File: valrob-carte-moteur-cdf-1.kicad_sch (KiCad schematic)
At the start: 0 parts

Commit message: schem: add ESP32-S3-WROOM-1 symbol
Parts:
- added U1: ESP32-S3-WROOM-1, PCM_Espressif:ESP32-S3-WROOM-1, symbol PCM_Espressif:ESP32-S3-WROOM-1
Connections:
- new net GND: U1.1 (GND), U1.40 (GND), U1.41 (GND)
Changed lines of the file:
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@@
 	(generator_version "9.0")
 	(paper "A4")
+	(wire
+		(pts
+			(xy 134.62 133.35) (xy 134.62 135.89)
+		)
+		(stroke
+			(width 0)
+			(type default)
+		)
+	)
+	(symbol
+		(lib_id "PCM_Espressif:ESP32-S3-WROOM-1")
+		(at 134.62 92.71 0)
+		(unit 1)
+		(exclude_from_sim no)
+		(in_bom yes)
+		(on_board yes)
+		(dnp no)
+		(fields_autoplaced yes)
+		(property "Reference" "U1"
+			(at 136.7633 49.53 0)
+			(effects
+				(font
+					(size 1.27 1.27)
+				)
+				(justify left)
+			)
+		)
+		(property "Value" "ESP32-S3-WROOM-1"
+			(at 136.7633 52.07 0)
+			(effects
+				(font
+					(size 1.27 1.27)
+				)
+				(justify left)
+			)
+		)
+		(property "Footprint" "PCM_Espressif:ESP32-S3-WROOM-1"
+			(at 137.16 140.97 0)
+			(effects
+				(font
+					(size 1.27 1.27)
+				)
+				(hide yes)
+			)
+		)
+		(property "Datasheet" "https://www.espressif.com/sites/default/files/documentation/esp32-s3-wroom-1_wroom-1u_datasheet_en.pdf"
+			(at 137.16 143.51 0)
+			(effects
+				(font
+					(size 1.27 1.27)
+				)
+				(hide yes)
+			)
+		)
+		(property "Description" "2.4 GHz WiFi (802.11 b/g/n) and Bluetooth ® 5 (LE) module Built around ESP32S3 series of SoCs, Xtensa ® dualcore 32bit LX7 microprocessor Flash up to 16 MB, PSRAM up to 8 MB 36 GPIOs, rich set of peripherals Onboard PCB antenna"
+			(at 134.62 92.71 0)
+			(effects
+				(font
+					(size 1.27 1.27)
+				)
+				(hide yes)
+			)
+		)
+		(pin "32"
+		)
+		(pin "2"
+		)
+		(pin "5"
+		)
+		(pin "1"
+		)
+		(pin "17"
+		)
+		(pin "31"
+		)
+		(pin "15"
+		)
+		(pin "19"
+		)
+		(pin "14"
+		)
+		(pin "20"
+		)
+		(pin "23"
+		)
+		(pin "30"
+		)
+		(pin "13"
+		)
+		(pin "3"
+		)
+		(pin "16"
+		)
+		(pin "25"
+		)
+		(pin "18"
+		)
+		(pin "4"
+		)
+		(pin "34"
+		)
+		(pin "33"
+		)
+		(pin "40"
+		)
+		(pin "6"
+		)
+		(pin "29"
+		)
+		(pin "8"
+		)
+		(pin "38"
+		)
+		(pin "36"
+		)
+		(pin "9"
+		)
+		(pin "22"
+		)
+		(pin "21"
+		)
+		(pin "12"
+		)
+		(pin "7"
+		)
+		(pin "11"
+		)
+		(pin "10"
+		)
+		(pin "24"
+		)
+		(pin "26"
+		)
+		(pin "28"
+		)
+		(pin "39"
+		)
+		(pin "41"
+		)
+		(pin "27"
+		)
+		(pin "35"
+		)
+		(pin "37"
+		)
+		(instances
+			(project ""
+				(path "/b89f538c-def5-4450-bb35-40e96c574400"
+					(reference "U1")
+					(unit 1)
+				)
+			)
+		)
+	)
+	(symbol
+		(lib_id "power:GND")
+		(at 134.62 135.89 0)
+		(unit 1)
+		(exclude_from_sim no)
+		(in_bom yes)
+		(on_board yes)
+		(dnp no)
+		(fields_autoplaced yes)
+		(property "Reference" "#PWR01"
+			(at 134.62 142.24 0)
+			(effects
+				(font
+					(size 1.27 1.27)
+				)
+				(hide yes)
+			)
+		)
+		(property "Value" "GND"
+			(at 134.62 140.97 0)
+			(effects
+				(font
+					(size 1.27 1.27)
+				)
+			)
+		)
+		(property "Footprint" ""
+			(at 134.62 135.89 0)
+			(effects
+				(font
+					(size 1.27 1.27)
+				)
+				(hide yes)
+			)
+		)
+		(property "Datasheet" ""
+			(at 134.62 135.89 0)
+			(effects
+				(font
+					(size 1.27 1.27)
+				)
+				(hide yes)
+			)
+		)
+		(property "Description" "Power symbol creates a global label with name \"GND\" , ground"
+			(at 134.62 135.89 0)
+			(effects
+				(font
+					(size 1.27 1.27)
+				)
+				(hide yes)
+			)
+		)
+		(pin "1"
+		)
+		(instances
+			(project ""
+				(path "/b89f538c-def5-4450-bb35-40e96c574400"
+					(reference "#PWR01")
+					(unit 1)
+				)
+			)
+		)
+	)
 	(sheet_instances
 		(path "/"

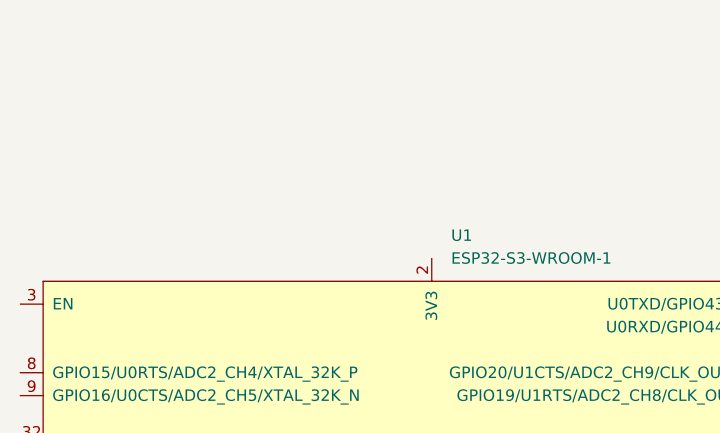
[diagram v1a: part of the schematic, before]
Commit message: schem: add ESP32 decoupling caps
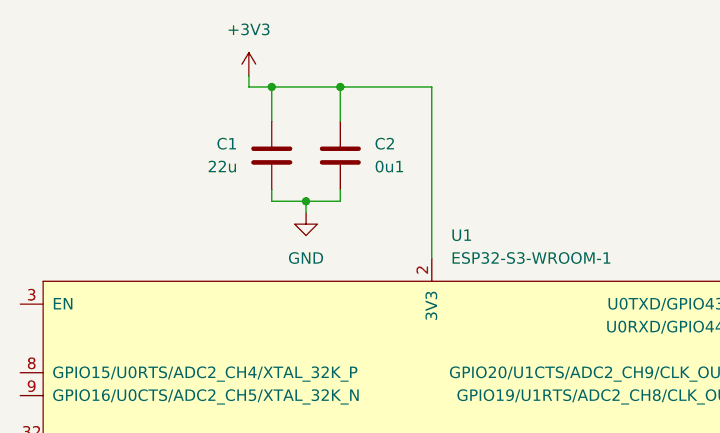
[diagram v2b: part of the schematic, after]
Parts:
- added C1: 22u, symbol Device:C
- added C2: 0u1, symbol Device:C
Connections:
- net GND: now also C1.2, C2.2
- net +3V3: now reaches U1.2 (3V3)
- net +3V3: now also C1.1, C2.1

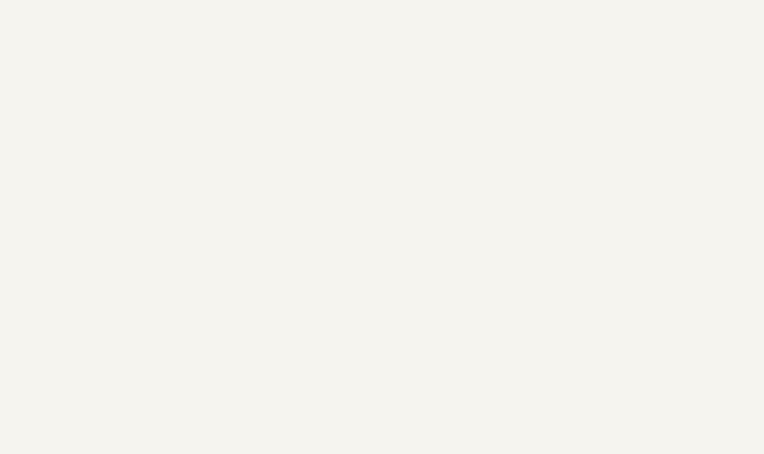
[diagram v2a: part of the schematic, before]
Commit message: schem: import AP2112K 3.3v from esp32c6-sensor-devboard
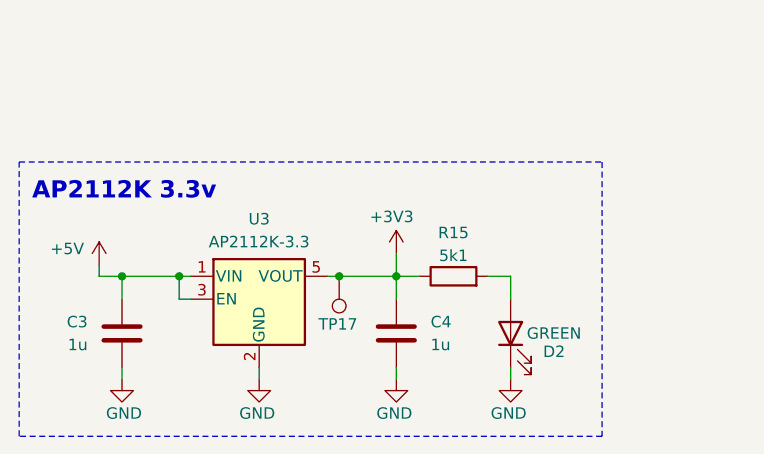
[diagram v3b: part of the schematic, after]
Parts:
- added C3, C4: 1u, Capacitor_SMD:C_0603_1608Metric, symbol Device:C
- added D2: GREEN, LED_SMD:LED_0805_2012Metric, symbol Device:LED
- added R15: 5k1, Resistor_SMD:R_0603_1608Metric, symbol Device:R
- added TP17: TestPoint, TestPoint:TestPoint_Pad_D2.0mm, symbol Connector:TestPoint
- added U3: AP2112K-3.3, Package_TO_SOT_SMD:SOT-23-5, symbol Regulator_Linear:AP2112K-3.3
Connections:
- net +3V3: now also C4.1, R15.1, TP17.1, U3.5 (VOUT)
- net GND: now also C3.2, C4.2, D2.1 (K), U3.2 (GND)
- new net: D2.2 (A), R15.2
- new net +5V: C3.1, U3.1 (VIN), U3.3 (EN)
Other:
- note added: "AP2112K 3.3v"

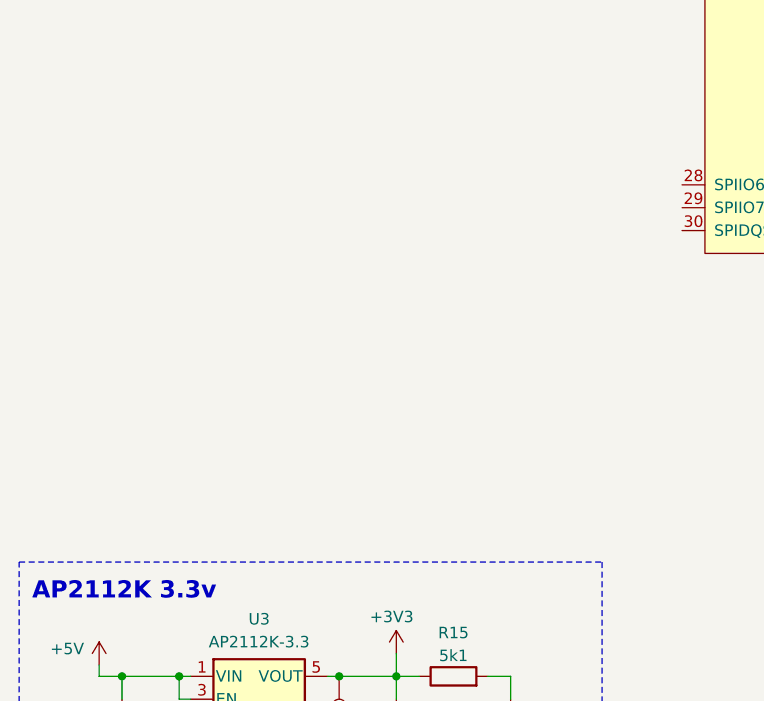
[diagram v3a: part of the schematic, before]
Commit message: schem: import USB-C from esp32c6-sensor-devboard
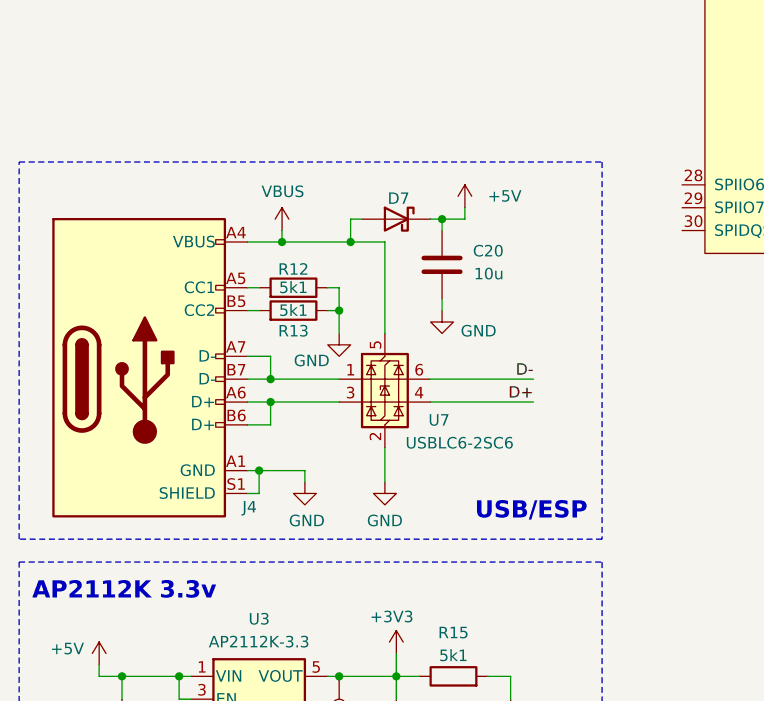
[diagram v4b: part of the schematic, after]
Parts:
- added C20: 10u, Capacitor_SMD:C_0402_1005Metric, symbol Device:C
- added D7: D_Schottky, Diode_SMD:D_SMA, symbol Device:D_Schottky
- added J4: USB_C_Receptacle_USB2.0_14P, Connector_USB:USB_C_Receptacle_HRO_TYPE-C-31-M-12, symbol Connector:USB_C_Receptacle_USB2.0_14P
- added R12, R13: 5k1, Resistor_SMD:R_0603_1608Metric, symbol Device:R
- added U7: USBLC6-2SC6, Package_TO_SOT_SMD:SOT-23-6, symbol Power_Protection:USBLC6-2SC6
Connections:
- net +5V: now also C20.1, D7.1 (K)
- net GND: now also C20.2, J4.A1 (GND), J4.A12 (GND), J4.B1 (GND), J4.B12 (GND), J4.S1 (SHIELD), R12.1, R13.1, U7.2 (GND)
- new net: J4.A5 (CC1), R12.2
- new net: J4.A6 (D+), J4.B6 (D+), U7.3 (I/O2)
- new net: J4.A7 (D-), J4.B7 (D-), U7.1 (I/O1)
- new net: J4.B5 (CC2), R13.2
- new net D+: U7.4 (I/O2)
- new net D-: U7.6 (I/O1)
- new net VBUS: D7.2 (A), J4.A4 (VBUS), J4.A9 (VBUS), J4.B4 (VBUS), J4.B9 (VBUS), U7.5 (VBUS)
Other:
- note added: "USB/ESP"

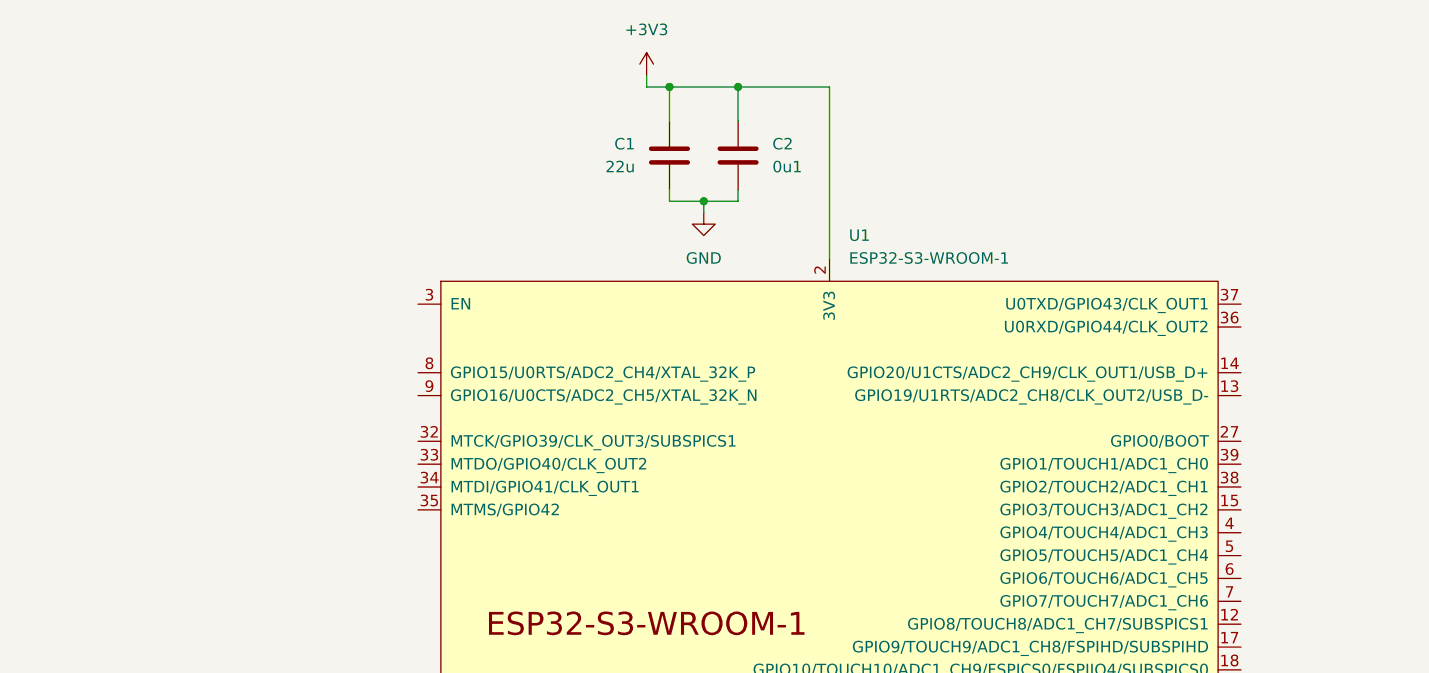
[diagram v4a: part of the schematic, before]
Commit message: schem: add BOOT and CHIP_PU strapping pullups
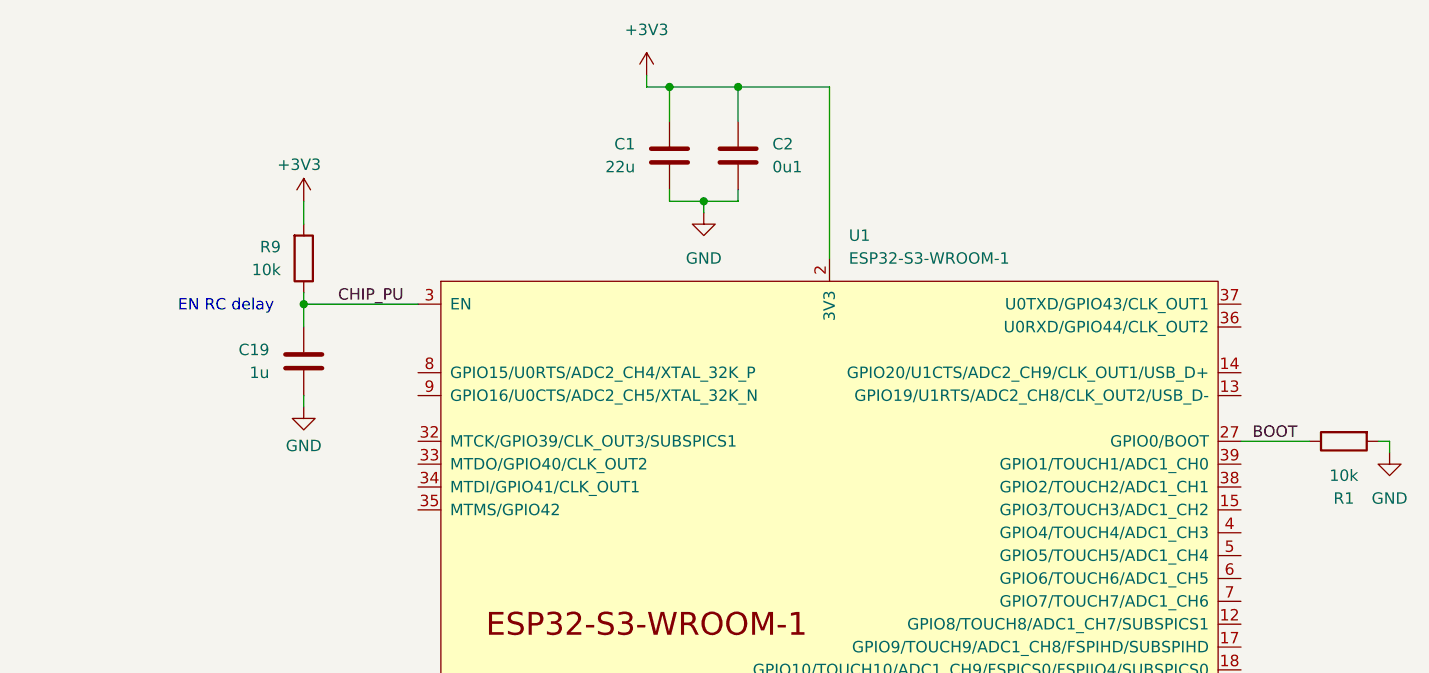
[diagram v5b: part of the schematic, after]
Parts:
- added C19: 1u, Capacitor_SMD:C_0402_1005Metric, symbol Device:C
- added R1, R9: 10k, Resistor_SMD:R_0603_1608Metric, symbol Device:R
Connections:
- net +3V3: now also R9.2
- net GND: now also C19.2, R1.2
- net BOOT: now reaches U1.27 (GPIO0/BOOT)
- net BOOT: now also R1.1
- net CHIP_PU: now reaches U1.3 (EN)
- net CHIP_PU: now also C19.1, R9.1
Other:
- note added: "EN RC delay"

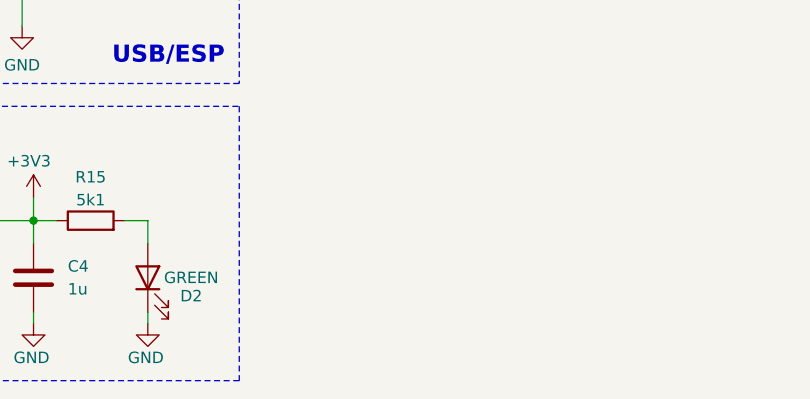
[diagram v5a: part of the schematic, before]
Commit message: schem: import boot and rst btns from esp32c6-sensor-devboard
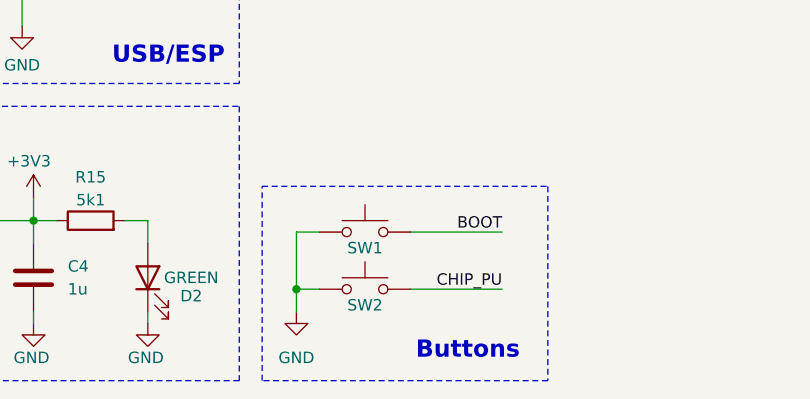
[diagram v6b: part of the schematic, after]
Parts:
- added SW1, SW2: SW_Push, Button_Switch_SMD:SW_SPST_TS-1088-xR020, symbol Switch:SW_Push
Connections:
- net BOOT: now also SW1.2
- net CHIP_PU: now also SW2.2
- net GND: now also SW1.1, SW2.1
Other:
- note added: "Buttons"

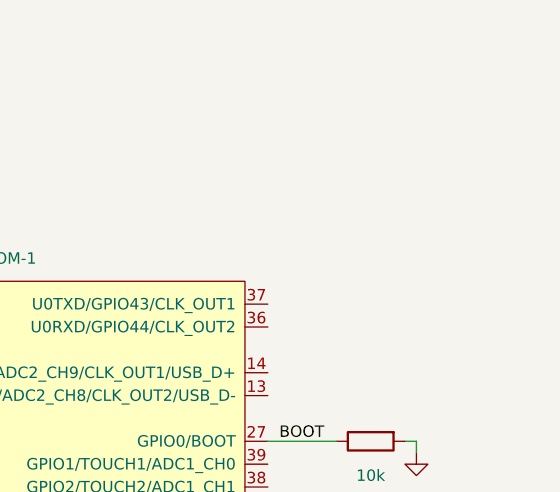
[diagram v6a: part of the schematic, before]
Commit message: schem: import UART connector without series resistor from esp32c6-sensor-devboard
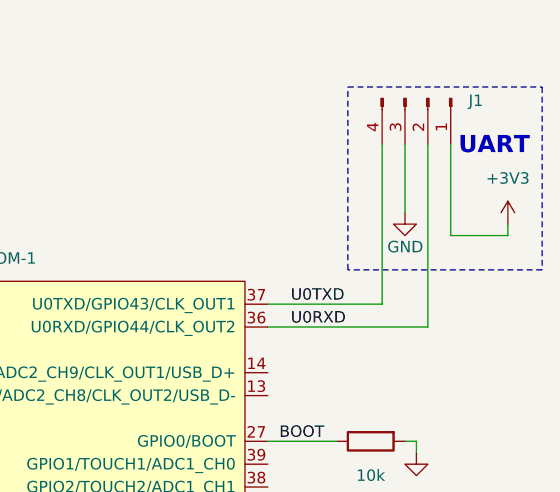
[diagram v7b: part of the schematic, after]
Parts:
- added J1: Conn_01x04_Pin, Connector_PinHeader_2.54mm:PinHeader_1x04_P2.54mm_Vertical, symbol Connector:Conn_01x04_Pin
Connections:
- net +3V3: now also J1.1 (Pin_1)
- net GND: now also J1.3 (Pin_3)
- net U0RXD: now reaches U1.36 (U0RXD/GPIO44/CLK_OUT2)
- net U0RXD: now also J1.2 (Pin_2)
- net U0TXD: now reaches U1.37 (U0TXD/GPIO43/CLK_OUT1)
- net U0TXD: now also J1.4 (Pin_4)
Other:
- note added: "UART"

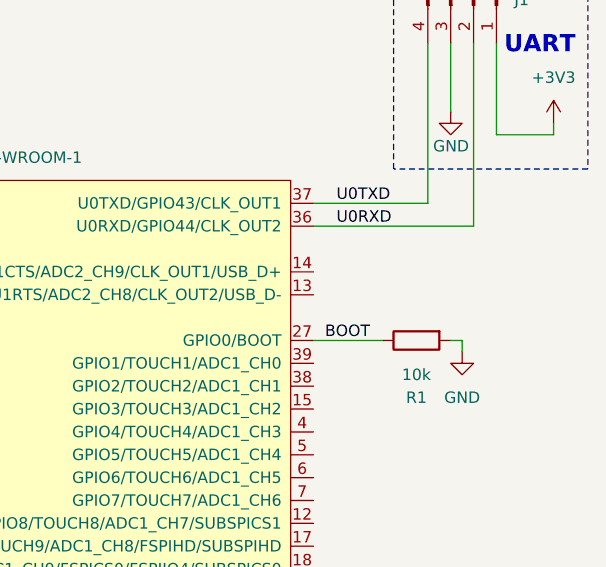
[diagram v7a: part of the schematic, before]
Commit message: schem: add USB termination resistors
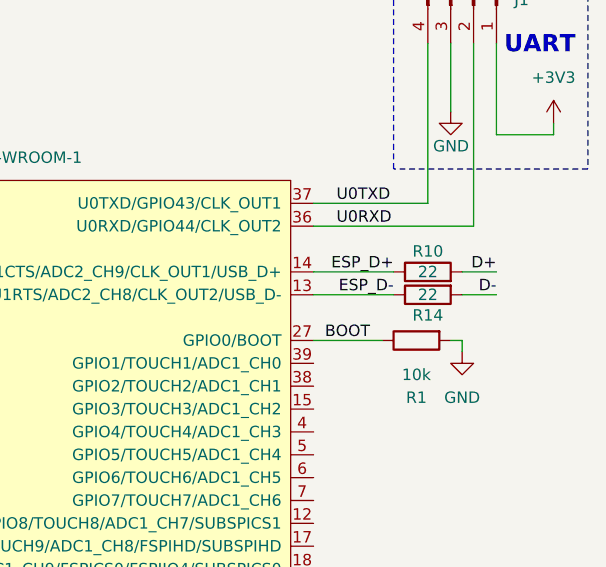
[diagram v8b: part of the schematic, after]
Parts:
- added R10, R14: 22, Resistor_SMD:R_0402_1005Metric, symbol Device:R
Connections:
- net D+: now also R10.2
- net D-: now also R14.2
- net ESP_D-: now reaches U1.13 (GPIO19/U1RTS/ADC2_CH8/CLK_OUT2/USB_D-)
- net ESP_D-: now also R14.1
- net ESP_D+: now reaches U1.14 (GPIO20/U1CTS/ADC2_CH9/CLK_OUT1/USB_D+)
- net ESP_D+: now also R10.1
